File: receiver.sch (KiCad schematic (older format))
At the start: 38 parts

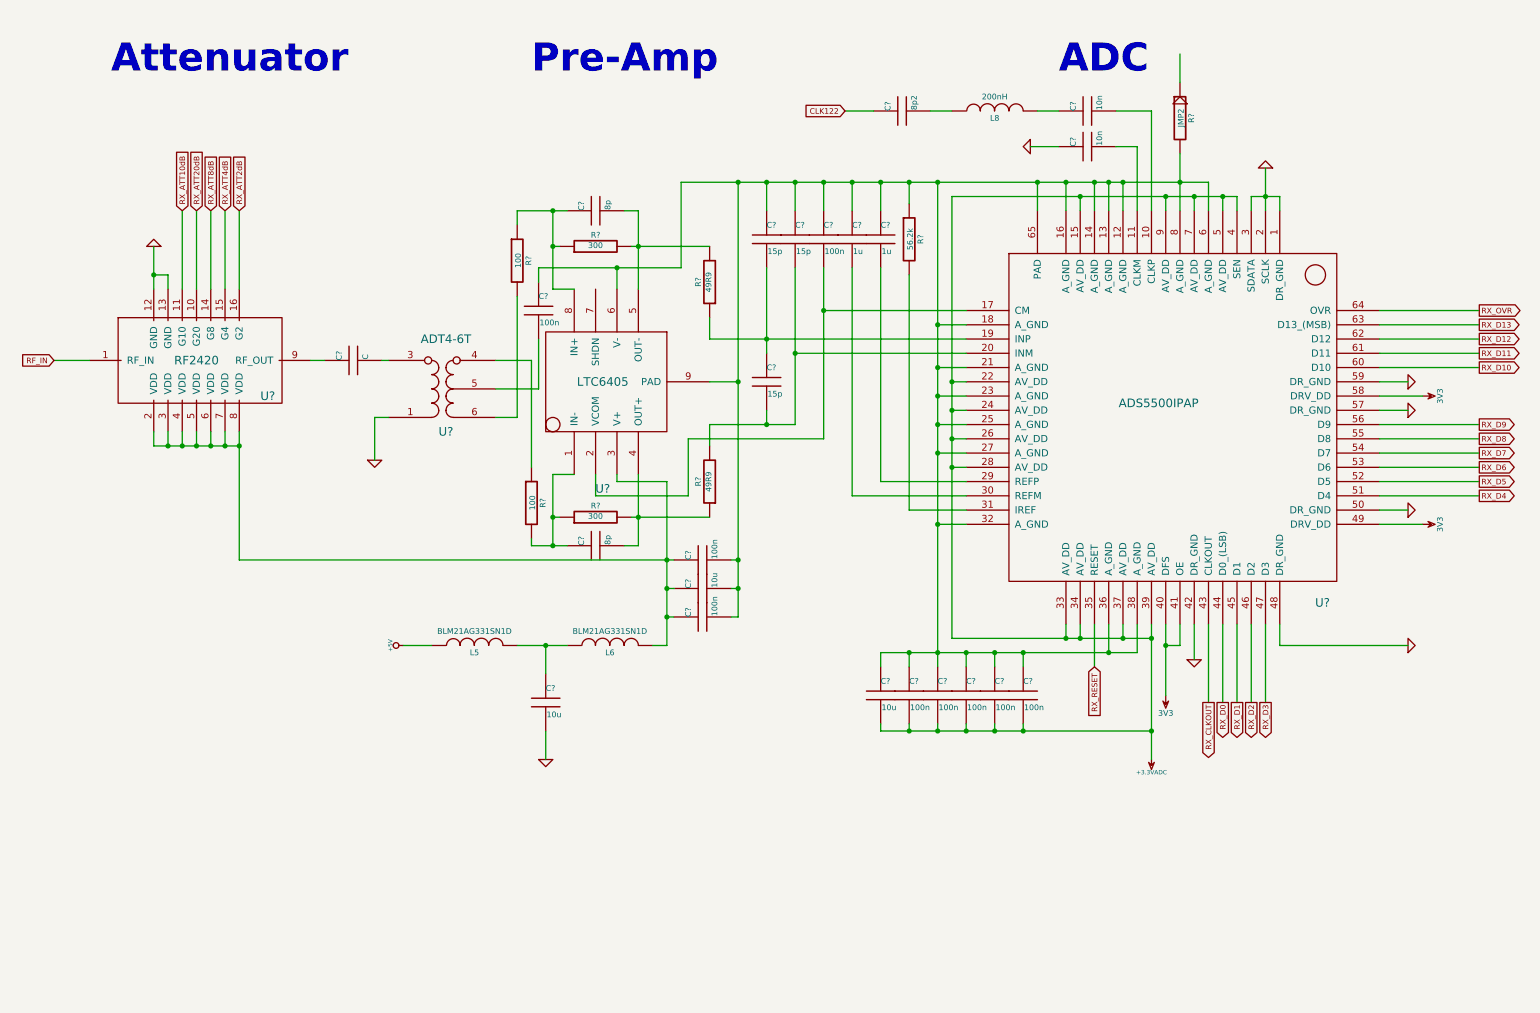
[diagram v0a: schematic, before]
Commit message: tx/rx section mostly complete
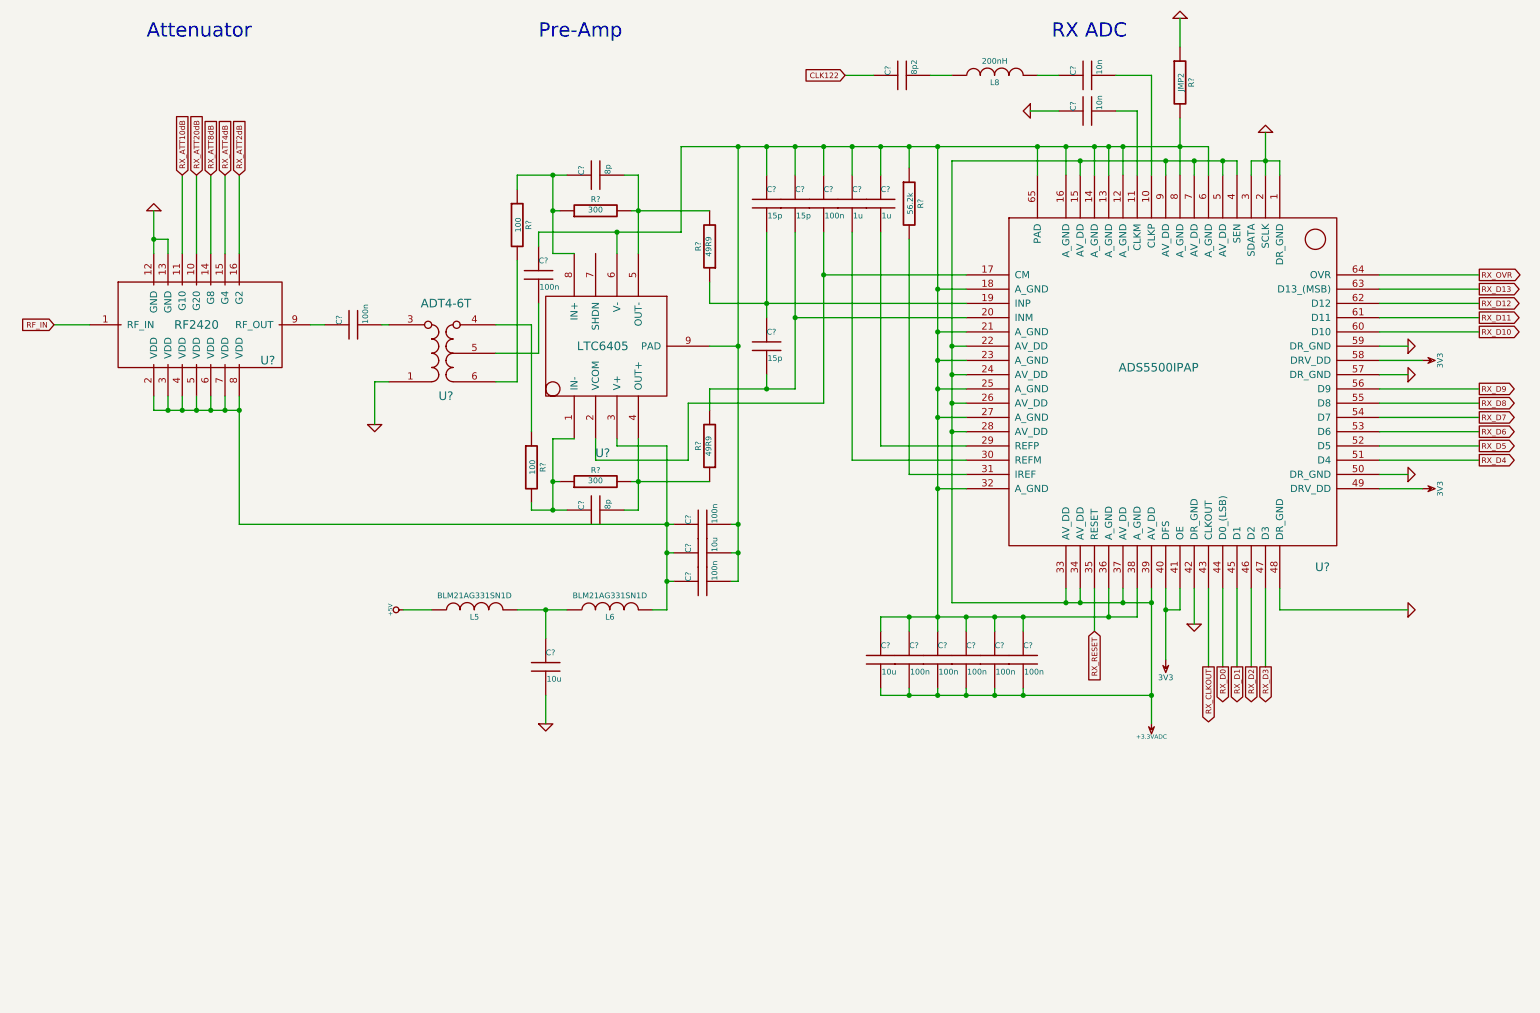
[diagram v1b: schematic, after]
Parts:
- C?: value C -> 100n
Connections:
- net GND: now also R?.1
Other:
- note added: "Pre-Amp"
- note added: "RX ADC"
- note removed: "ADC"
- note removed: "Pre-Amp\n"
- moved on the sheet: C?, L5, L6, L8, R?, U?

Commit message: finished rx section started on power
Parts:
- added C? (x2): 100n, ~, symbol C
- added D?: BAT64-05, symbol BAT64-05
- added R?: 220k, ~, symbol R
- added U?: RX_IN, symbol SMA
- added U?: AUX_IN, symbol SMA
- added U?: PB1103CT-ND, symbol PB1103CT-ND
- added U?: GBLC03C, symbol GBLC03C
- added U?: BCR148W, symbol BCR148W
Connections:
- net +5V: now also U?.1
- net GND: now also D?.1, D?.2, R?.2, U?.10, U?.12, U?.13, U?.15, U?.17, U?.19, U?.2, U?.2, U?.2, U?.2, U?.2, U?.21, U?.22, U?.3, U?.3, U?.5, U?.7
- net RF_IN: now also C?.2
- new net: U?.1, U?.20
- new net: U?.1, U?.14
- new net: D?.3, U?.11, U?.3
- new net: C?.1, R?.1, U?.6
- new net: C?.1, C?.2, U?.1
- new net RX_ANTSWITCH: U?.1
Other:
- note added: "Antenna Switch"

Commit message: additions and fixes
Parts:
- removed L5, L6: BLM21AG331SN1D, ~, symbol INDUCTOR
- added R? (x2): 10, symbol R
- C? (x2): value 10u -> 22uF
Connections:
- net +5V: now also R?.2
- net at C?.1, C?.1, C?.1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: now also R?.1
- net at C?.1: now also R?.1, R?.2
